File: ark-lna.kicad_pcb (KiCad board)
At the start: 2 copper layers, 18 parts, among them P1 CONN_1, P2 CONN_1, P3 CONN_2, U1 LM1117-5, U2 MAR-6+

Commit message: Minor cleanups
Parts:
- moved L2 2.54 mm to (134.6, 113.0)
- moved C4 2.01 mm to (133.3, 116.2)
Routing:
- net Net-(C3-Pad1): track 9.52 -> 7.22 mm
- net Net-(C7-Pad2): track 5.84 -> 4.05 mm
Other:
- board outline added: 50 x 46.5 mm

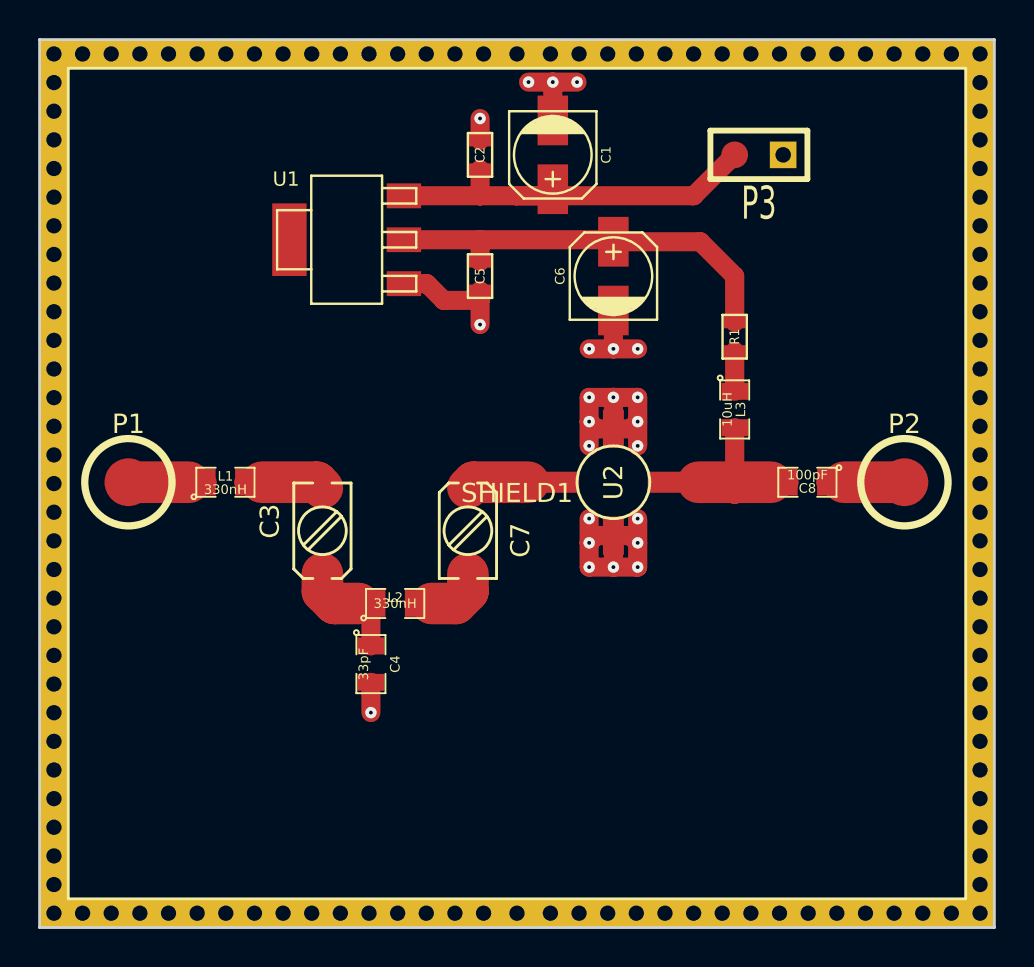
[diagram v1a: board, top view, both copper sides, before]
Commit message: finishing touches on silkscreen
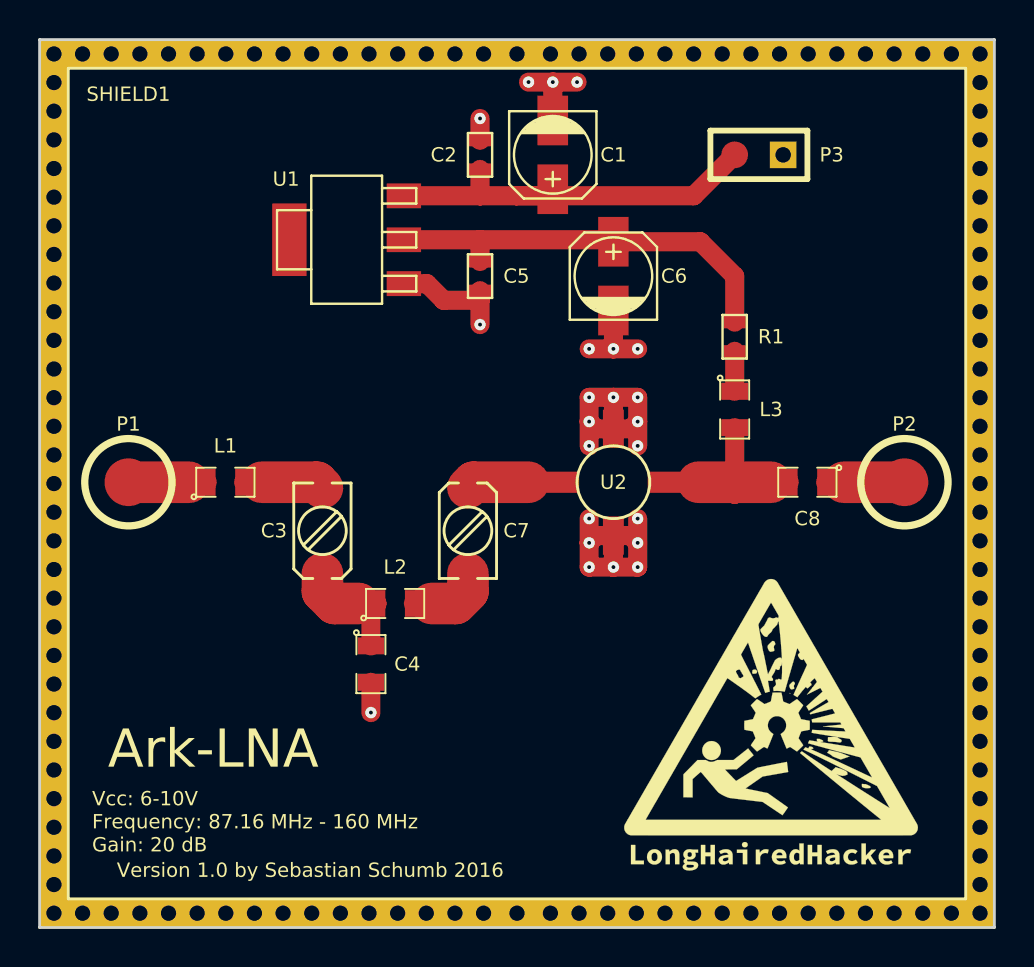
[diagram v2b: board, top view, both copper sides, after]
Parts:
- added G***: LOGO, misc:logo, F.Cu at (154.3, 119.4)
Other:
- board text added: "Ark-LNA"
- board text added: "Vcc: 6-10V Frequency: 87.16 MHz - 160 MHz Gain: 20 dB"
- board text added: "Version 1.0 by Sebastian Schumb 2016"

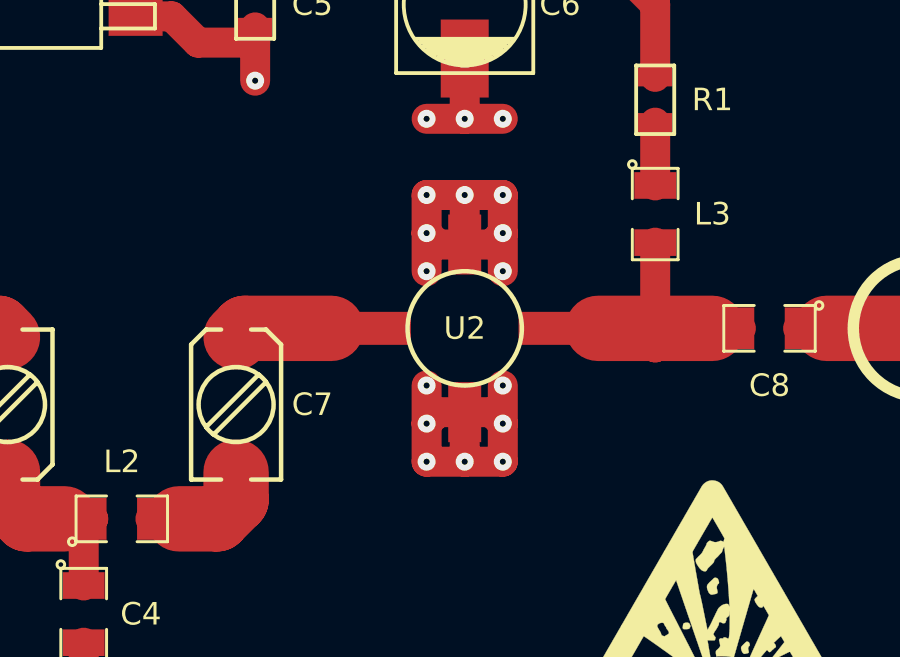
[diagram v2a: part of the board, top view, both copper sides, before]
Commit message: Fixed footprint for MAR-6
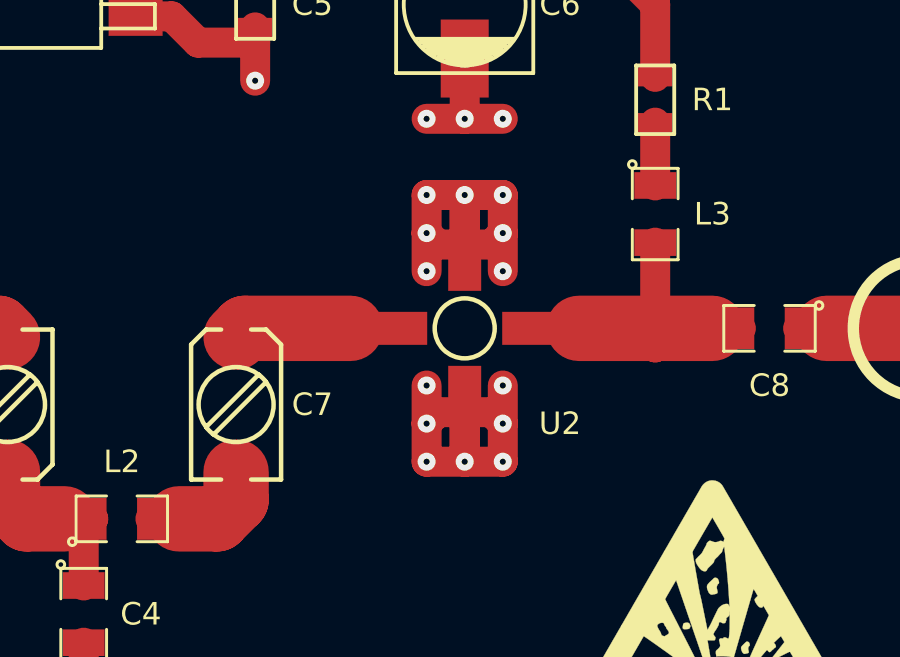
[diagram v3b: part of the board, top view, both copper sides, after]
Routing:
- net GND: track 42.2 -> 46.6 mm
